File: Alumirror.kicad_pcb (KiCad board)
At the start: 2 copper layers, 139.7 x 88.9 mm, 96 parts, among them J1 USB_C_Receptacle_USB2.0_16P_2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, J2 USB_C_Receptacle_USB2.0_16P_2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, J3 USB_C_Receptacle_USB2.0_16P_2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, J4 USB_C_Receptacle_USB2.0_16P_2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, K00 PG1350, K01 PG1350, K02 PG1350, K03 PG1350, K04 PG1350, K05 PG1350, K10 PG1350, K11 PG1350, K12 PG1350, K13 PG1350, K14 PG1350, K15 PG1350, K20 PG1350, K21 PG1350, K22 PG1350, K23 PG1350, K24 PG1350, K25 PG1350_1½U, K30 PG1350_1½U, K31 PG1350/SKQUCAA010, SW1 BOOT, U1 CH552T, U2 CH552T, U3 USBLC6-2P6, U4 USBLC6-2P6, U5 USBLC6-2P6, U6 USBLC6-2P6

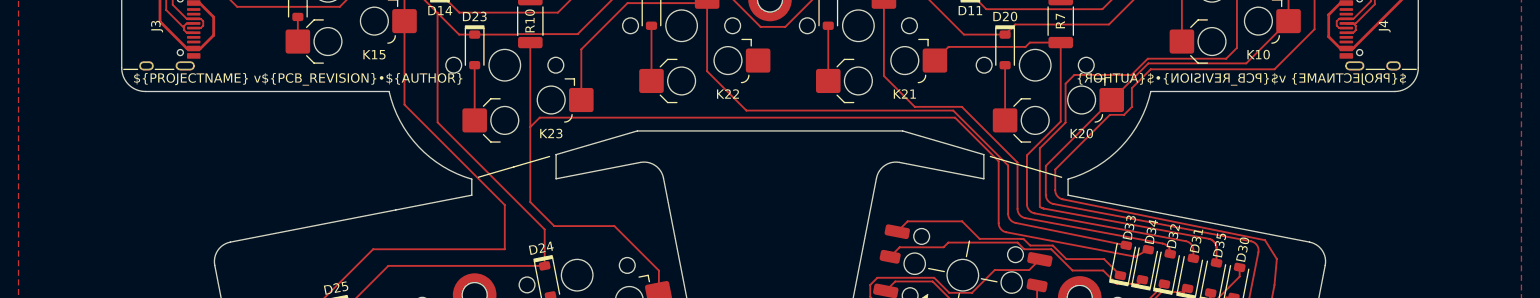
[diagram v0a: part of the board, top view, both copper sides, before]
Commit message: Clean up edges around thumb keys
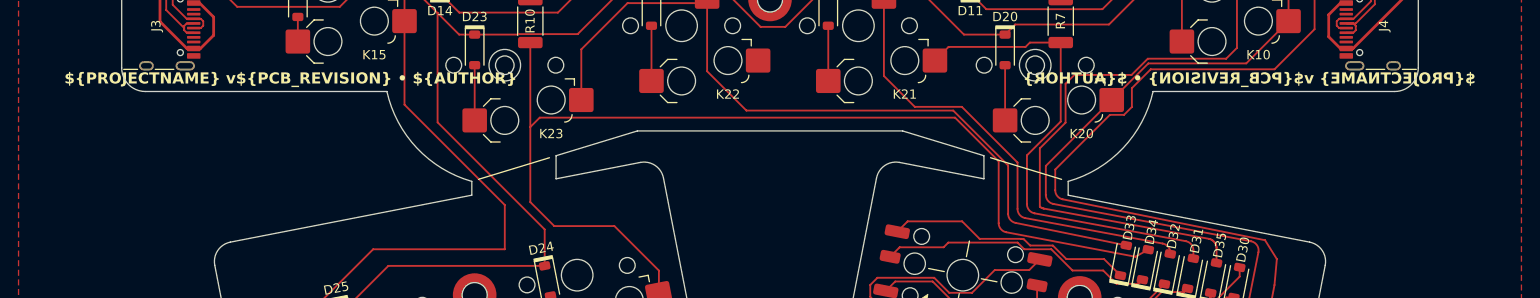
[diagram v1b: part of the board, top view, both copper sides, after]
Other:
- outline, holes or cut-outs redrawn
- board text added: "${PROJECTNAME} v${PCB_REVISION} • ${AUTHOR}"
- board text removed: "${PROJECTNAME} v${PCB_REVISION}•${AUTHOR}"

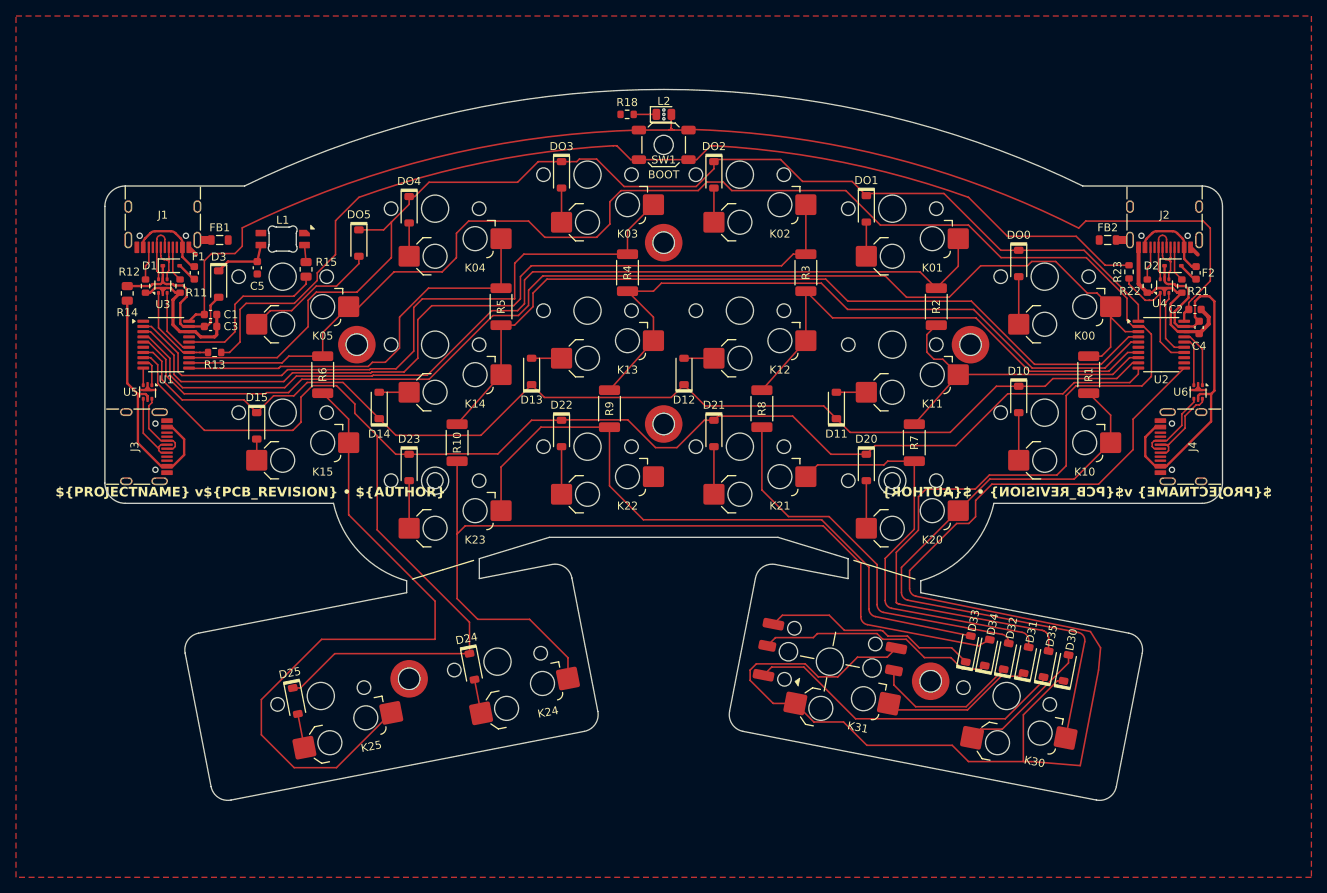
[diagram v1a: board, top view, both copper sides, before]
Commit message: Switch R14 back to 2010 size
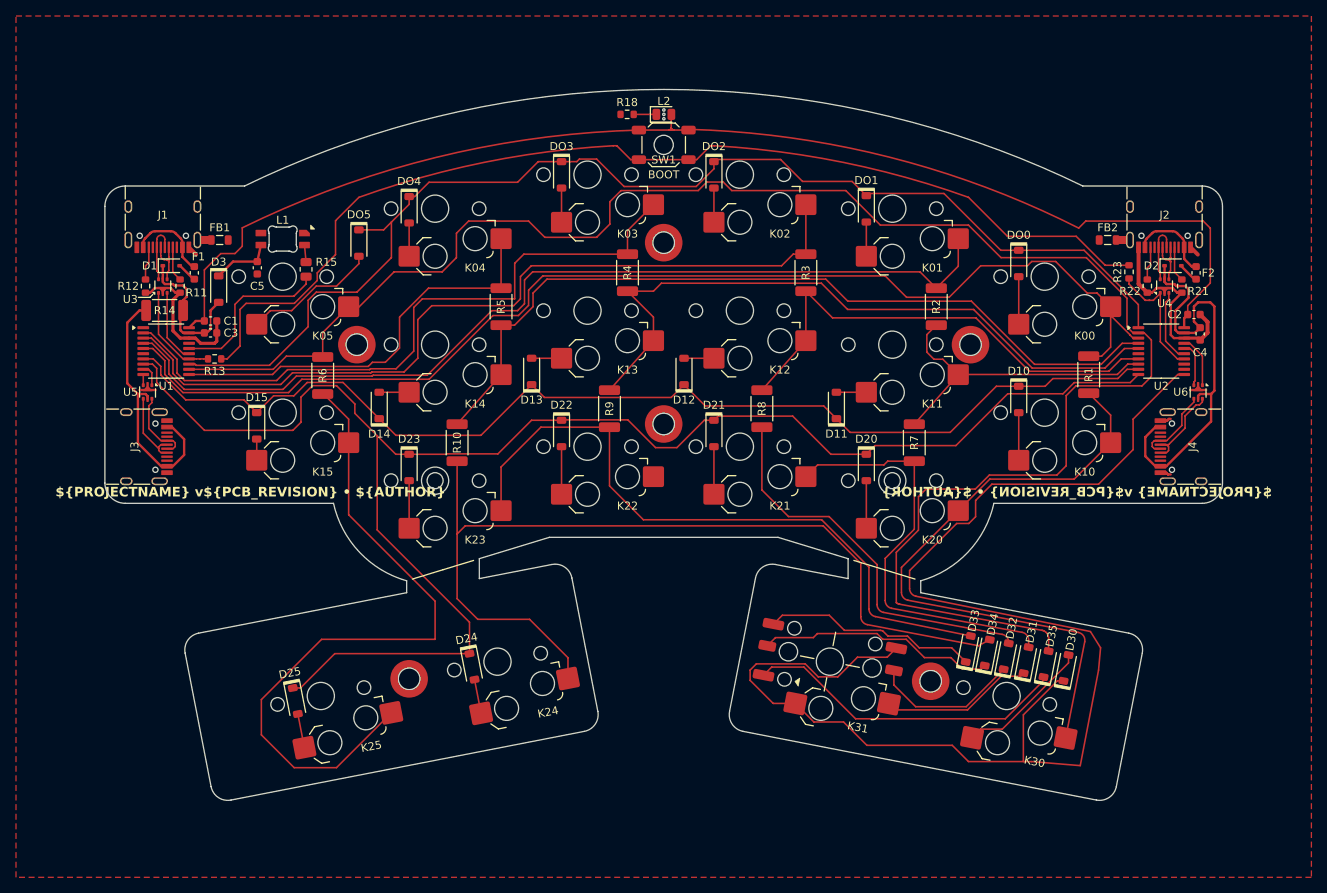
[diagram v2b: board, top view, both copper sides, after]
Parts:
- R14: footprint Resistor_SMD:R_0805_2012Metric -> Resistor_SMD:R_2010_5025Metric
- moved R14 5.14 mm to (90.0, 56.6), turned to 180 degrees
- moved C4 0.82 mm to (219.5, 59.6)
- moved C1 0.81 mm to (95.8, 58.0)
- moved C3 0.81 mm to (95.8, 59.4)
- moved NT1 0.81 mm to (94.4, 62.7)
- moved R13 0.81 mm to (96.3, 62.7)
- moved U1 0.81 mm to (90.2, 61.7)
- moved U2 0.81 mm to (214.6, 61.7)
- moved C2 0.65 mm to (218.7, 57.1)
- moved D3 0.63 mm to (96.8, 54.0)
- moved R6 0.10 mm to (109.8, 64.8)
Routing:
- net GND: track 42.0 -> 46.5 mm
- net VCC_L: track 22.3 -> 17.9 mm
- net Col0: track 151.1 -> 149.6 mm
- net Row2: track 205.5 -> 204.0 mm
- net Row1: track 143.2 -> 141.8 mm
- net Row0: track 150.9 -> 152.2 mm
- net TX_L: track 3.67 -> 2.82 mm
- net RX_R: track 7.42 -> 6.59 mm
- net +3V3: track 54.4 -> 55.2 mm
- net USB_L+: track 10.3 -> 11.1 mm
- net USB_L-: track 8.36 -> 9.17 mm
- net RX_L: track 2.14 -> 1.33 mm
- net VCC_R: track 52.4 -> 53.2 mm
- net TX_R: track 6.32 -> 5.65 mm
- net BOOT: track 68.3 -> 68.9 mm
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
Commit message: Shuffle components around again and fix DRC messages
 * Move split connection ESD chip to inside of associated USB port instead of above.
 * Scootch MCUs down.
 * Reduce clearance of ESD chip ground pin polygon pad.
 * Change solder nut hole to through-hole pad instead of NPT hole and solid pad.
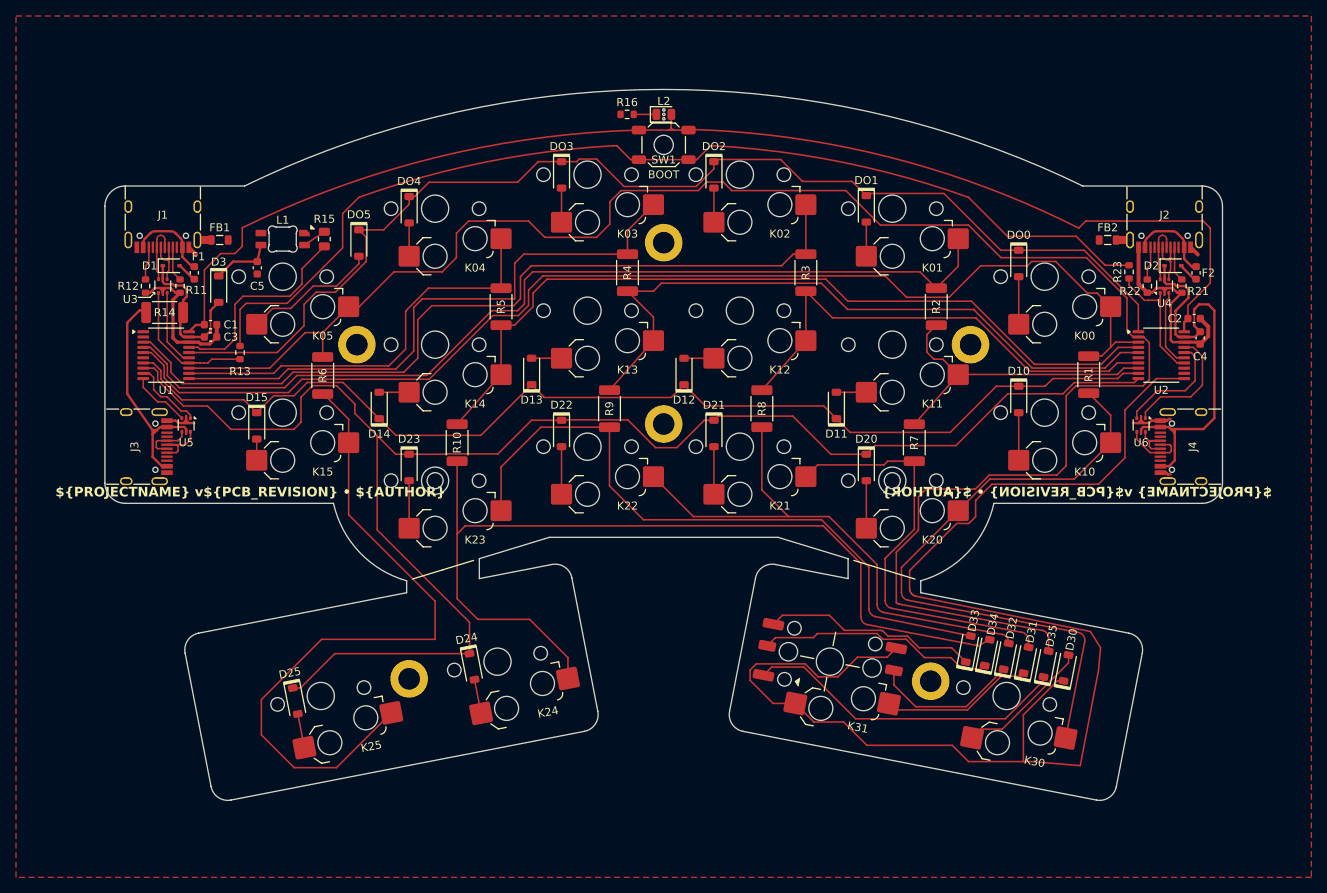
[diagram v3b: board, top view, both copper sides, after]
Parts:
- moved U6 8.23 mm to (212.1, 71.0)
- moved U5 6.35 mm to (92.7, 71.0)
- moved R15 4.42 mm to (110.0, 47.7)
- moved R13 3.27 mm to (99.4, 61.9), turned to 90 degrees
- moved C3 0.51 mm to (95.8, 60.0)
- moved C4 0.51 mm to (219.5, 60.1)
- moved NT1 0.51 mm to (94.4, 63.2)
- moved U1 0.51 mm to (90.2, 62.2)
- moved U2 0.51 mm to (214.6, 62.2)
- moved C2 0.50 mm to (218.7, 57.7)
- moved C1 0.46 mm to (95.8, 58.4)
- moved R14 0.26 mm to (90.0, 56.9)
- moved NT2 0.12 mm to (213.0, 55.4)
- renumbered R18 to R16
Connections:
- J3 pad A6: RX_PL -> TX_PL
- J3 pad A7: TX_PL -> RX_PL
- J3 pad B6: RX_PL -> TX_PL
- J3 pad B7: TX_PL -> RX_PL
- J4 pad A6: TX_PR -> RX_PR
- J4 pad A7: RX_PR -> TX_PR
- J4 pad B6: TX_PR -> RX_PR
- J4 pad B7: RX_PR -> TX_PR
- U1 pad 11: Col4L -> Col3L
- U1 pad 12: Col5 -> Col4L
- U1 pad 13: Row0 -> Col5
- U1 pad 16: LED -> Row0
- U1 pad 17: unconnected-(U1-P1.2-Pad17) -> LED
- U1 pad 2: Col3L -> unconnected-(U1-P1.4-Pad2)
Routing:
- net Col2RT: track 48.9 -> 67.8 mm
- net Col3L: track 83.9 -> 74.6 mm
- net RX_R: track 6.59 -> 15.6 mm
- net TX_R: track 5.65 -> 14.3 mm
- net TX_L: track 2.82 -> 9.35 mm
- net RX_L: track 1.33 -> 7.53 mm
- net RX_PR: track 11.5 -> 6.24 mm
- net LED: track 21.1 -> 26.0 mm
- net Net-(NT1-Pad2): track 0.51 -> 4.70 mm
- net Row0: track 152.2 -> 148.1 mm
- net VCC_L': track 32.6 -> 28.6 mm
- net RX_PL: track 9.77 -> 6.19 mm
- net BOOT: track 68.9 -> 65.4 mm
- net GND: track 46.5 -> 49.7 mm
- net TX_PR: track 10.2 -> 8.08 mm
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
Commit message: Renumber components
 * For single-digit components:
   * Odd numbers are populated on the lefthand board only
   * Even numbers are populated on the righthand board only
 * Double-digit components are populated on both sides
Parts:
- renumbered L2 to L10, R11 to R1, R16 to R10, R1 to R11, R2 to R12, R3 to R13, R4 to R14, R5 to R15, R6 to R16, R7 to R17, R8 to R18, R9 to R19, R21 to R2, R10 to R20, R12 to R3, R22 to R4, R13 to R5, R23 to R6, R14 to R7, R15 to R9, SW1 to SW10

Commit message: Renumber matrix switches and diodes
Columns and rows start from 1 rather than 0.
All components now follow the rules from the previous change, and we don’t had to mess around with the fake D-“oh” nonsense.
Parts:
- renumbered DO0 to D11, DO1 to D12, DO2 to D13, DO3 to D14, DO4 to D15, DO5 to D16, D10 to D21, D11 to D22, D12 to D23, D13 to D24, D14 to D25, D15 to D26, D20 to D31, D21 to D32, D22 to D33, D23 to D34, D24 to D35, D25 to D36, D30 to D41, D31 to D42, D32 to D43, D33 to D44, D34 to D45, D35 to D46, K00 to K11, K01 to K12, K02 to K13, K03 to K14, K04 to K15, K05 to K16, K10 to K21, K11 to K22, K12 to K23, K13 to K24, K14 to K25, K15 to K26, K20 to K31, K21 to K32, K22 to K33, K23 to K34, K24 to K35, K25 to K36, K30 to K41, K31 to K42
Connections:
- net Col0 renamed Col1
- net Col0T renamed Col1T
- net Col5 renamed Col6
- net Row3R renamed Row4R
- D11 pad 1: Row0 -> Row1
- D12 pad 1: Row0 -> Row1
- D13 pad 1: Row0 -> Row1
- D14 pad 1: Row0 -> Row1
- D15 pad 1: Row0 -> Row1
- D16 pad 1: Row0 -> Row1
- D21 pad 1: Row1 -> Row2
- D22 pad 1: Row1 -> Row2
- D23 pad 1: Row1 -> Row2
- D24 pad 1: Row1 -> Row2
- D25 pad 1: Row1 -> Row2
- D26 pad 1: Row1 -> Row2
- D31 pad 1: Row2 -> Row3
- D32 pad 1: Row2 -> Row3
- D33 pad 1: Row2 -> Row3
- D34 pad 1: Row2 -> Row3
- D35 pad 1: Row2 -> Row3
- D36 pad 1: Row2 -> Row3
- D42 pad 2: Col1RT -> Col2RT
- D43 pad 2: Col2RT -> Col3RT
- D44 pad 2: Col3RT -> Col4RT
- D45 pad 2: Col4T -> Col5T
- K12 pad 1: Col1L -> Col2L
- K13 pad 1: Col2L -> Col3L
- K14 pad 1: Col3L -> Col4L
- K15 pad 1: Col4L -> Col5L
- K22 pad 1: Col1R -> Col2R
- K23 pad 1: Col2R -> Col3R
- K24 pad 1: Col3R -> Col4R
- K25 pad 1: Col4R -> Col5R
- K26 pad 1: Col5T -> Col6T
- K32 pad 1: Col1RT -> Col2RT
- K33 pad 1: Col2RT -> Col3RT
- K34 pad 1: Col3RT -> Col4RT
- K35 pad 1: Col4T -> Col5T
- K36 pad 1: Col5T -> Col6T
- R12 pad 1: Col1L -> Col2L
- R12 pad 2: Col1R -> Col2R
- R13 pad 1: Col2L -> Col3L
- R13 pad 2: Col2R -> Col3R
- R14 pad 1: Col3L -> Col4L
- R14 pad 2: Col3R -> Col4R
- R15 pad 1: Col4L -> Col5L
- R15 pad 2: Col4R -> Col5R
- R16 pad 2: Col5T -> Col6T
- R17 pad 1: Col1R -> Col2R
- R17 pad 2: Col1RT -> Col2RT
- R18 pad 1: Col2R -> Col3R
- R18 pad 2: Col2RT -> Col3RT
- R19 pad 1: Col3R -> Col4R
- R19 pad 2: Col3RT -> Col4RT
- R20 pad 1: Col4R -> Col5R
- R20 pad 2: Col4T -> Col5T
- U1 pad 11: Col3L -> Col4L
- U1 pad 12: Col4L -> Col5L
- U1 pad 16: Row0 -> Row1
- U1 pad 3: Col2L -> Col3L
- U1 pad 4: Col1L -> Col2L
- U1 pad 7: Row1 -> Row2
- U1 pad 8: Row2 -> Row3
- U2 pad 1: Row0 -> Row1
- U2 pad 10: Row2 -> Row3
- U2 pad 4: Col4R -> Col5R
- U2 pad 5: Col3R -> Col4R
- U2 pad 7: Col2R -> Col3R
- U2 pad 8: Col1R -> Col2R
- U2 pad 9: Row1 -> Row2
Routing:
- net Row3: track 0.00 -> 203.1 mm
- net Row0: track 148.1 -> 0.00 mm
- net Col1L: track 118.0 -> 0.00 mm
- net Col4T: track 113.3 -> 0.00 mm
- net Col5R: track 0.00 -> 102.8 mm
- net Col6T: track 0.00 -> 86.6 mm
- net Col4RT: track 0.00 -> 83.8 mm
- net Row2: track 203.1 -> 141.4 mm
- net Col1RT: track 53.4 -> 0.00 mm
- net Col5L: track 0.00 -> 52.4 mm
- net Col1R: track 40.0 -> 0.00 mm
- net Col3L: track 74.6 -> 103.0 mm
- net Col5T: track 86.6 -> 113.3 mm
- net Col3R: track 85.3 -> 60.6 mm
- net Col4L: track 52.4 -> 74.6 mm
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
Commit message: Update resistor values
Testing seemed to show that 5.1KΩ will work well for a dim power LED.
The value for the boot resistor is not well defined, but values from 5.1KΩ to 20KΩ have been seem.
(Using 5.1KΩ for these means that the same resistor stock used for USB power control can be used.)
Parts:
- R10: value 10k -> 5k1
- R5: value 10k -> 5k1–20k
- R6: value 10k -> 5k1-20k
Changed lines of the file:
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@@
 			)
 		)
-		(property "Value" "10k"
+		(property "Value" "5k1–20k"
 			(at 0 1.43 90)
 			(layer "F.Fab")
@@
 			)
 		)
-		(property "Value" "10k"
+		(property "Value" "5k1-20k"
 			(at 0 1.43 90)
 			(layer "F.Fab")
@@
 			)
 		)
-		(property "Value" "10k"
+		(property "Value" "5k1"
 			(at 0 1.43 180)
 			(layer "F.Fab")

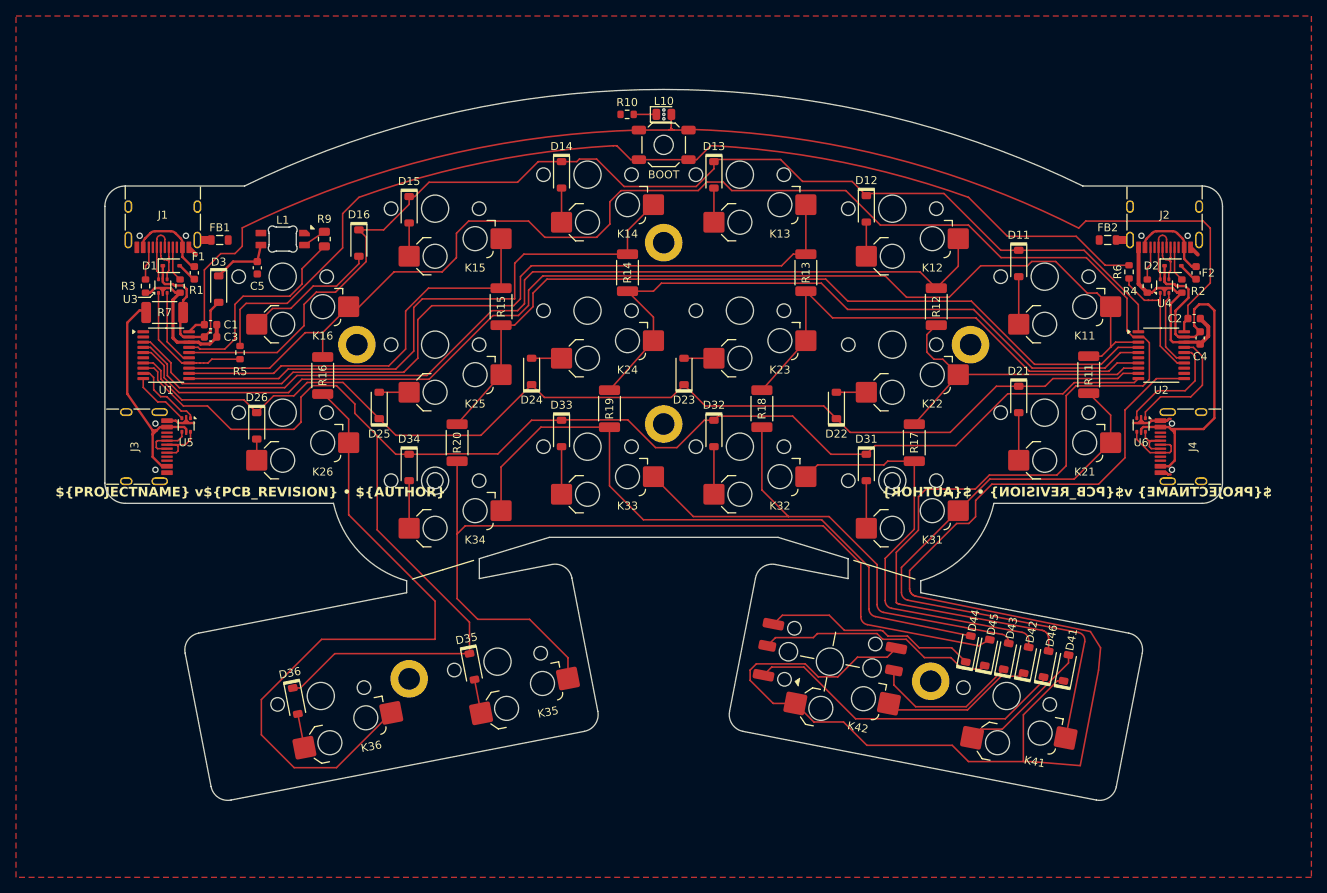
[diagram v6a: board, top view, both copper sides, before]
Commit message: Start to clean up traces
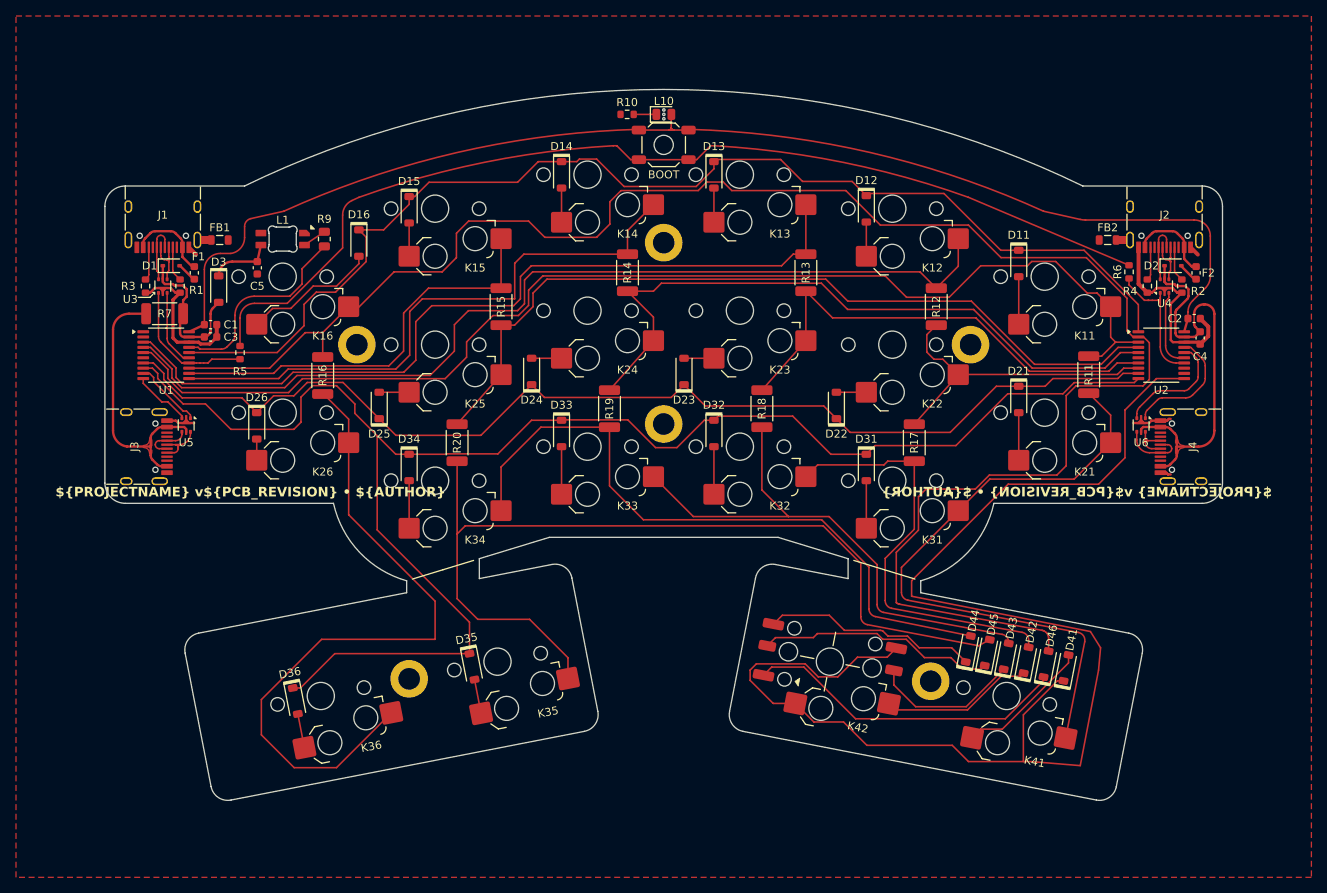
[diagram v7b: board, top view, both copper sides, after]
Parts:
- moved R7 0.15 mm to (90.0, 57.0)
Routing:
- net +3V3: track 56.2 -> 65.5 mm
- net VCC_L': track 28.6 -> 34.1 mm
- net BOOT: track 65.4 -> 63.4 mm
- net Row4R: track 172.3 -> 170.3 mm
- net TX_PL: track 7.69 -> 5.82 mm
- net Col2L: track 118.0 -> 119.7 mm
- net RX_PR: track 6.24 -> 5.49 mm
- net VCC_L: track 19.3 -> 18.6 mm
- net LED: track 26.0 -> 25.3 mm
- net TX_L: track 9.35 -> 8.75 mm
- net Col1: track 148.3 -> 148.9 mm
- added copper zone on F.Cu, net VCC_L'
- added copper zone on F.Cu, net VCC_R
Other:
- outline, holes or cut-outs redrawn
